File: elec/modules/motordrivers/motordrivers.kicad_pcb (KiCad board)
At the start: 2 copper layers, 40.6 x 61 mm, 16 parts, among them IC2 VNH5019ATR-E, J1 Conn_01x02, J10 Conn_01x05, J2 Conn_01x05, J9 Conn_01x05, Q1 AON6354

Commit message: fuction  more impt!
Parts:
- moved R8 7.07 mm to (135.3, 96.9), turned to 0 degrees
- moved C16 6.18 mm to (138.3, 101.9)
- moved R12 6.13 mm to (136.3, 101.9)
- moved R15 4.29 mm to (131.3, 98.9), turned to 180 degrees
- moved R9 4.24 mm to (135.3, 98.9), turned to 0 degrees
- moved R10 2.00 mm to (134.3, 101.9)
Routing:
- net /M SW: track 19.4 -> 0.00 mm, vias 4 -> 0
- net +3V3: track 24.9 -> 10.7 mm, vias 2 -> 0
- net Net-(C15-Pad1): track 13.8 -> 0.00 mm, vias 29 -> 28
- net Net-(IC2-INA): track 11.7 -> 0.00 mm
- net /M PWM: track 10.2 -> 0.00 mm
- net /M IN A: track 9.26 -> 0.00 mm
- net /CPM1: track 9.05 -> 0.00 mm, vias 2 -> 1
- net Net-(IC2-ENA/DIAGA): track 8.00 -> 0.00 mm
- net /M IN B: track 7.58 -> 0.00 mm
- net Net-(IC2-PWM): track 7.16 -> 0.00 mm, vias 2 -> 1
- net Net-(IC2-ENB/DIAGB): track 7.08 -> 0.20 mm, vias 2 -> 1
- net Net-(IC2-INB): track 6.66 -> 0.25 mm
- net GND: vias 294 -> 60

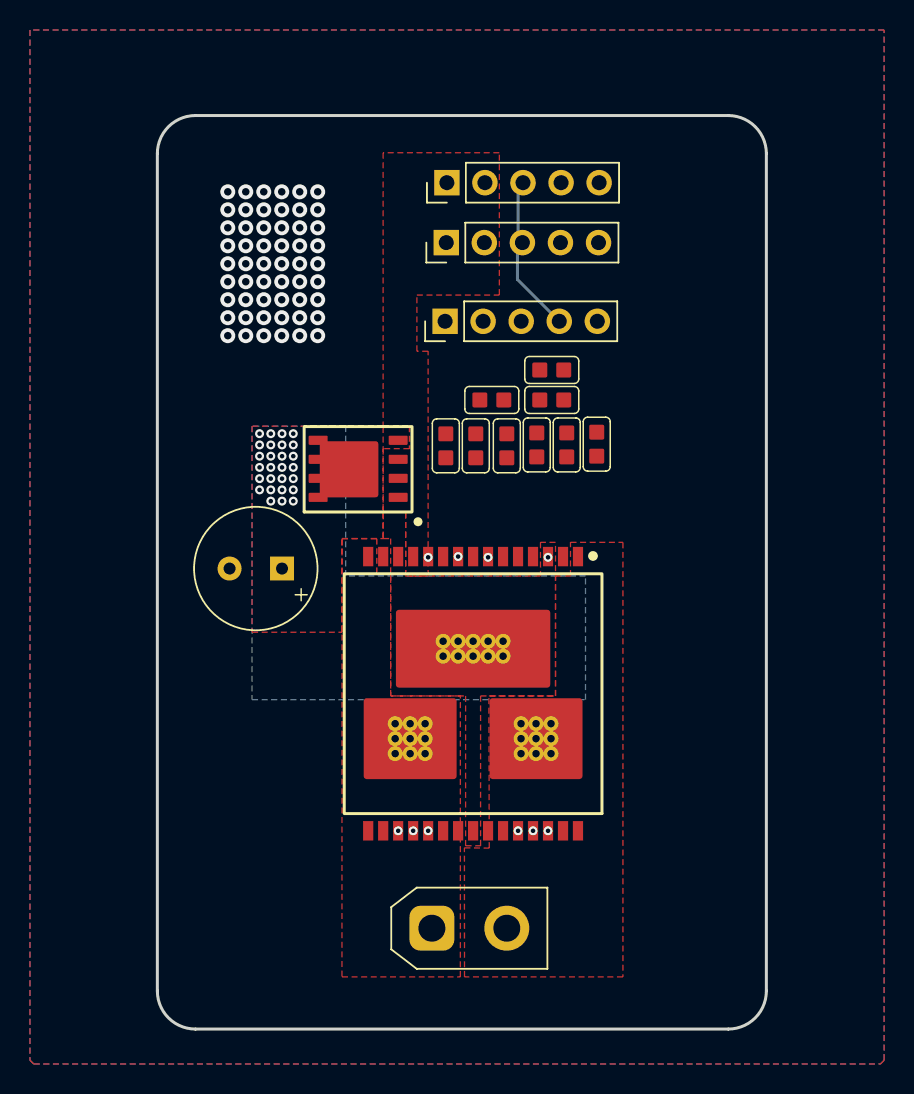
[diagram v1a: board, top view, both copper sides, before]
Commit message: did motor driver example
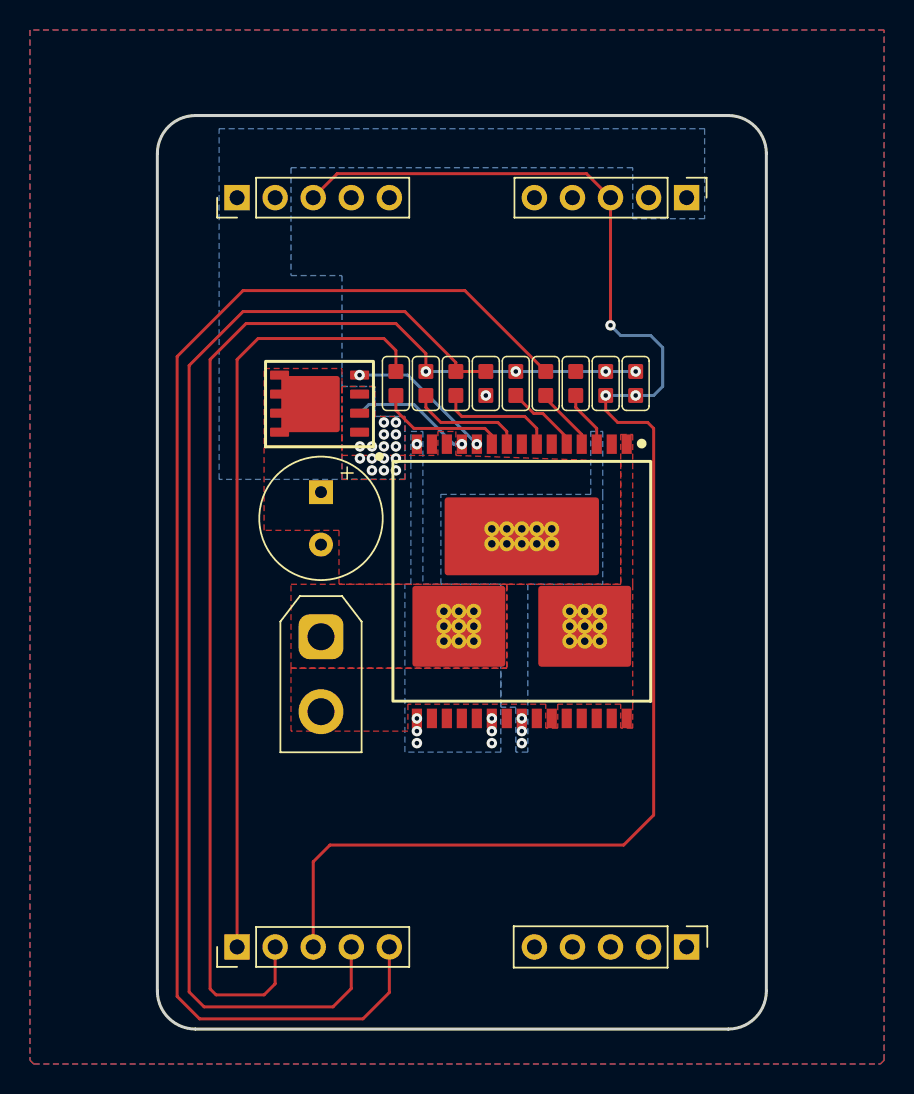
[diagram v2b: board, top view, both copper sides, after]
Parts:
- added J3: Conn_01x05, Connector_PinHeader_2.54mm:PinHeader_1x05_P2.54mm_Vertical, F.Cu at (144.3, 135.4)
- moved J9 44.0 mm to (114.3, 135.4)
- moved J1 20.8 mm to (119.9, 114.7), turned to -90 degrees
- moved J2 16.3 mm to (144.3, 85.4), turned to -90 degrees
- moved J10 14.0 mm to (114.3, 85.4)
- moved IC2 8.17 mm to (133.3, 111.0)
- moved R9 5.71 mm to (140.9, 97.8), turned to -90 degrees
- moved C15 5.49 mm to (119.9, 106.8), turned to -90 degrees
- moved R14 5.37 mm to (128.9, 97.8)
- moved R11 5.33 mm to (126.9, 97.8)
- moved R13 5.33 mm to (124.9, 97.8)
- moved Q1 5.06 mm to (119.8, 99.2)
- moved R10 4.33 mm to (132.9, 97.8)
- moved R12 4.33 mm to (134.9, 97.8)
- moved C16 4.29 mm to (136.9, 97.8)
- moved R8 3.71 mm to (138.9, 97.8), turned to -90 degrees
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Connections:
- J9 pad 2: /M PWM -> /M SW
- J9 pad 3: /M SW -> +3V3
- J9 pad 4: +3V3 -> /M PWM
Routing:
- net +3V3: track 10.7 -> 100.9 mm, vias 0 -> 3
- net /M IN A: track 0.00 -> 89.9 mm
- net /M SW: track 0.00 -> 80.7 mm, vias 0 -> 4
- net /M PWM: track 0.00 -> 79.6 mm
- net /M IN B: track 0.00 -> 52.1 mm
- net /CPM1: track 0.00 -> 9.73 mm, vias 1 -> 2
- net Net-(IC2-INB): track 0.25 -> 8.68 mm
- net +12V: track 0.00 -> 8.15 mm, vias 0 -> 16
- net Net-(IC2-PWM): track 0.00 -> 7.95 mm, vias 1 -> 0
- net Net-(IC2-ENB/DIAGB): track 0.20 -> 7.71 mm, vias 1 -> 0
- net Net-(IC2-ENA/DIAGA): track 0.00 -> 5.01 mm
- net Net-(IC2-INA): track 0.00 -> 4.24 mm
- net Net-(C15-Pad1): track 0.00 -> 3.83 mm, vias 28 -> 3
- net GND: vias 60 -> 1
- net /OUT B M: vias 0 -> 7
- added copper zone on B.Cu, net +12V
- added copper zone on B.Cu, net /OUT B M

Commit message: i think thats drivers done
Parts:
- removed J10, J9: Conn_01x05, Pinheaders:PinHeader_1x05_P2.54mm_Vertical
- J2: value Conn_01x05 -> Conn_01x08; footprint Pinheaders:PinHeader_1x05_P2.54mm_Vertical -> Pinheaders:PinHeader_1x08_P2.54mm_Vertical
- J3: value Conn_01x05 -> Conn_01x08; footprint Connector_PinHeader_2.54mm:PinHeader_1x05_P2.54mm_Vertical -> Pinheaders:PinHeader_1x08_P2.54mm_Vertical
- moved J3 22.9 mm to (123.0, 127.0), turned to 90 degrees
- moved J2 3.68 mm to (140.7, 86.2)
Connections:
- J2 pad 1: +12V -> GND
- J2 pad 2: +12V -> /M IN A
- J2 pad 3: +3V3 -> /M SW
- J2 pad 4: GND -> +3V3
- J2 pad 5: GND -> +3V3
- J3 pad 1: unconnected-(J3-Pin_1-Pad1) -> +12V
- J3 pad 2: unconnected-(J3-Pin_2-Pad2) -> +12V
- J3 pad 3: unconnected-(J3-Pin_3-Pad3) -> +12V
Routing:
- net +3V3: track 100.9 -> 22.7 mm, vias 3 -> 2
- net /M IN A: track 89.9 -> 12.2 mm
- net /M PWM: track 79.6 -> 13.2 mm
- net /M SW: track 80.7 -> 26.0 mm
- net /M IN B: track 52.1 -> 11.1 mm, vias 0 -> 2
- net +12V: track 8.15 -> 0.00 mm, vias 16 -> 12
- net /CPM1: track 9.73 -> 11.0 mm
- net Net-(IC2-PWM): track 7.95 -> 7.24 mm
- net GND: vias 1 -> 2
- net /OUT B M: vias 7 -> 5

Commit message: aligned pogos
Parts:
- moved J2 17.7 mm to (123.0, 86.2), turned to 90 degrees
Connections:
- J2 pad 2: /M IN A -> /M IN B
- J2 pad 3: /M SW -> /M PWM
- J2 pad 6: /M PWM -> /M SW
- J2 pad 7: /M IN B -> /M IN A
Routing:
- net /M IN B: vias 2 -> 0
- net +12V: vias 12 -> 14

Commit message: sleepy but did most pcbs
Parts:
- moved J2 2.53 mm to (120.5, 86.2)
- moved J3 2.53 mm to (120.5, 127.0)
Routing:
- net +3V3: track 22.7 -> 25.1 mm
- net /M SW: track 26.0 -> 25.0 mm
- net /M IN A: track 12.2 -> 11.2 mm
- net /M PWM: track 13.2 -> 14.2 mm
- net /M IN B: track 11.1 -> 11.6 mm
- net GND: vias 2 -> 1

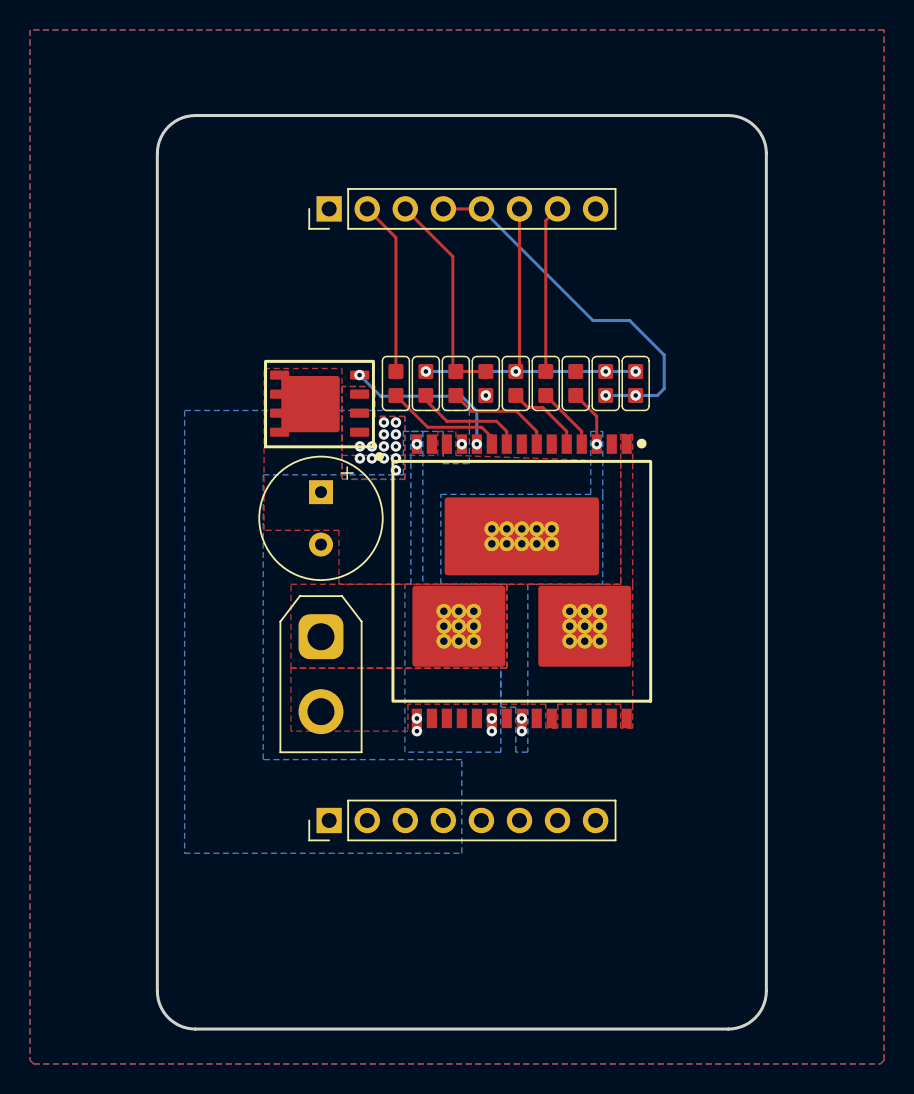
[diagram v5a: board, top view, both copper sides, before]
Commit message: motor drivers completed
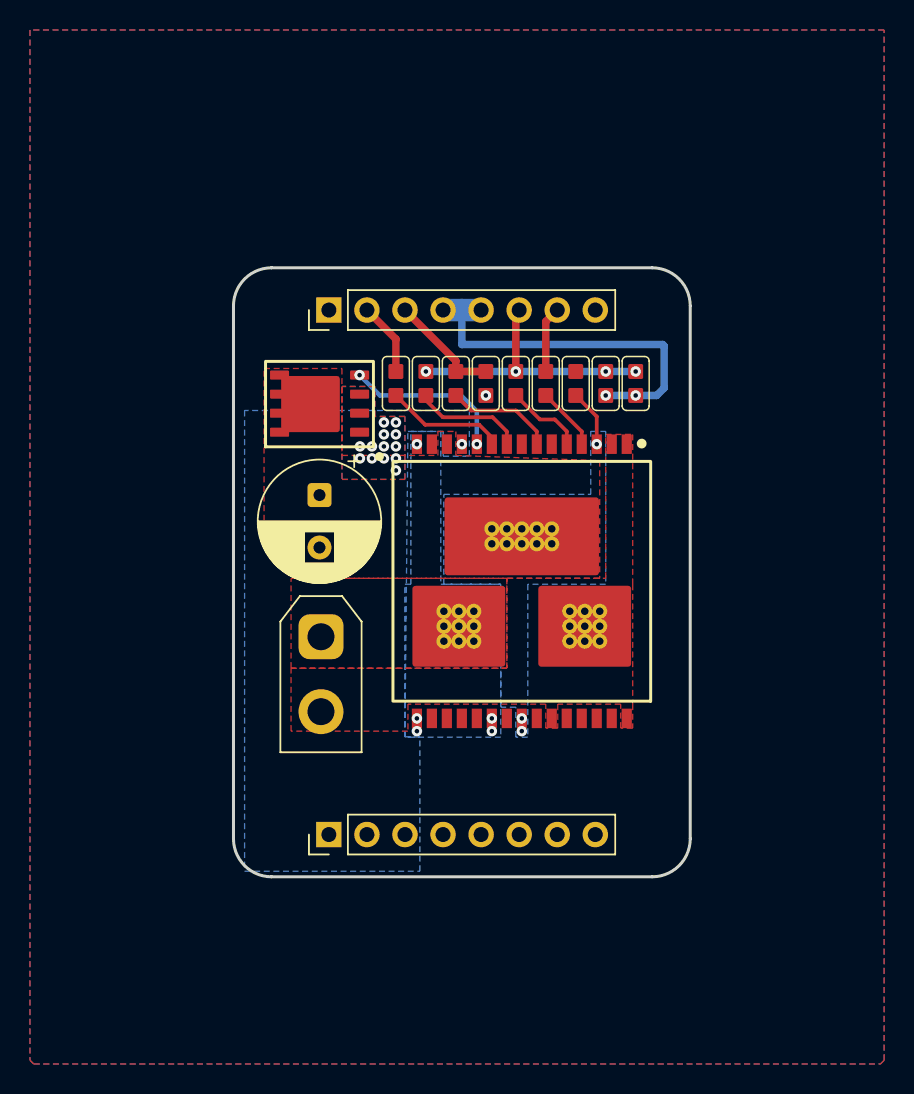
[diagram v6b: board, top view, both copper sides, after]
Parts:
- C15: footprint drivers:CP_Radial_D8.0mm_P3.50mm -> Capacitor_THT:CP_Radial_D8.0mm_P3.50mm
- C16: footprint drivers:cap0603 -> footprints:Capacitor_0603
- R10, R11, R12, R13, R14, R15, R8, R9: footprint drivers:res0603 -> footprints:Resistor_0603
- moved J2 11.1 mm to (129.3, 92.9)
- moved J3 8.90 mm to (129.3, 127.9)
- moved C15 1.56 mm to (119.8, 105.3)
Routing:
- net /M SW: track 25.0 -> 18.2 mm
- net /M IN A: track 11.2 -> 4.42 mm
- net /M IN B: track 11.6 -> 4.90 mm
- net /M PWM: track 14.2 -> 7.51 mm
- net Net-(IC2-INB): track 8.60 -> 8.01 mm
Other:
- board size 40.6 x 61 mm -> 30.5 x 40.6 mm
- board text added: "design of 2-Chairs. 2025 JLC Order No. JLCJLCJLCJLC"
